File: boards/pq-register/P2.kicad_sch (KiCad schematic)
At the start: 36 parts, among them Q12 T1-N652, Q13 T1-N652, Q14 T1-N652, Q15 T1-N652, Q16 T1-N652, Q17 T1-N652

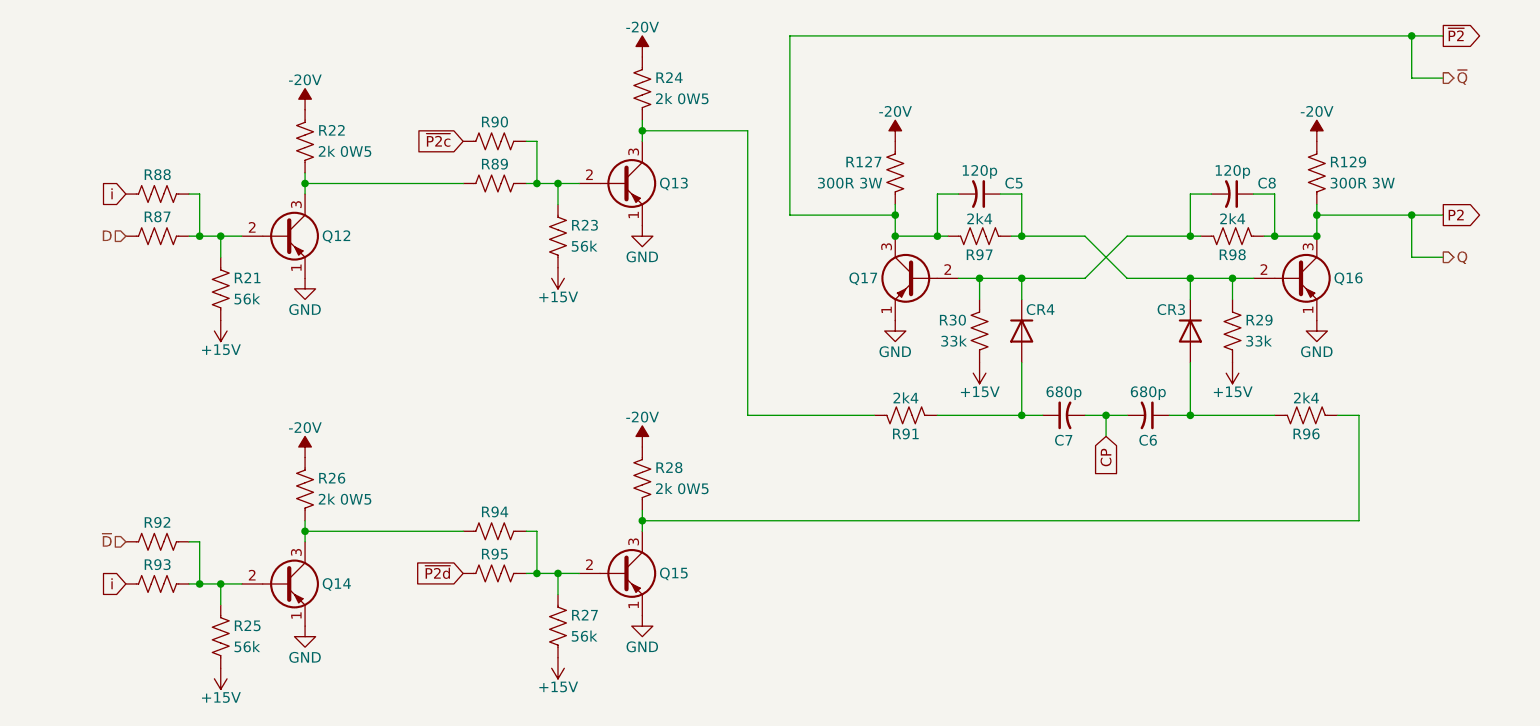
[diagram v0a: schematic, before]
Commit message: Run ERC and clean up P & Q Register board.
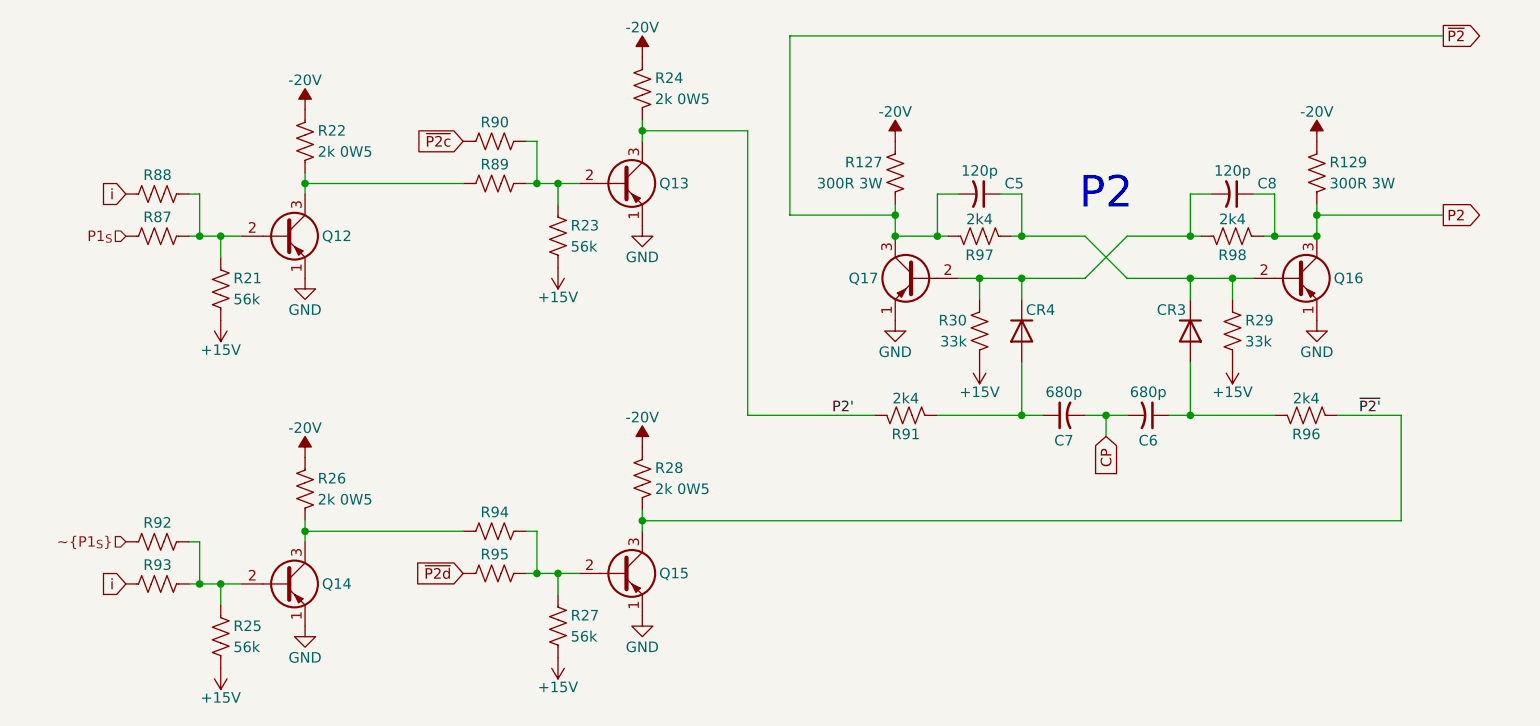
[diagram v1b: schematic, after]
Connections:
- net P2': now reaches Q13.3 (C), R24.2, R91.1
- net ~{P2'}: now reaches Q15.3 (C), R28.2, R96.2
- net D renamed P1_{S}
- net ~{D} renamed ~{P1_{S}}
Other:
- note added: "P2"
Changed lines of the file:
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@@
 		(title "LGP-21 P & Q Register Board")
 	)
+	(text "P2"
+		(exclude_from_sim no)
+		(at 177.8 82.55 0)
+		(effects
+			(font
+				(size 3.81 3.81)
+			)
+		)
+	)
 	(junction
 		(at 187.96 109.22)
@@
 	)
 	(junction
-		(at 214.63 85.09)
-		(diameter 0)
-		(color 0 0 0 0)
-	)
-	(junction
 		(at 167.64 87.63)
 		(diameter 0)
@@
 	)
 	(junction
-		(at 214.63 63.5)
-		(diameter 0)
-		(color 0 0 0 0)
-	)
-	(junction
 		(at 162.56 92.71)
 		(diameter 0)
@@
 	(wire
 		(pts
-			(xy 218.44 68.58) (xy 214.63 68.58)
-		)
-		(stroke
-			(width 0)
-			(type default)
-		)
-	)
-	(wire
-		(pts
 			(xy 180.34 87.63) (xy 187.96 87.63)
 		)
@@
 	(wire
 		(pts
-			(xy 218.44 90.17) (xy 214.63 90.17)
-		)
-		(stroke
-			(width 0)
-			(type default)
-		)
-	)
-	(wire
-		(pts
 			(xy 68.58 129.54) (xy 71.12 129.54)
 		)
@@
 	(wire
 		(pts
-			(xy 214.63 63.5) (xy 139.7 63.5)
+			(xy 139.7 63.5) (xy 218.44 63.5)
 		)
 		(stroke
@@
 	(wire
 		(pts
-			(xy 218.44 63.5) (xy 214.63 63.5)
-		)
-		(stroke
-			(width 0)
-			(type default)
-		)
-	)
-	(wire
-		(pts
 			(xy 139.7 63.5) (xy 139.7 85.09)
 		)
@@
 	(wire
 		(pts
-			(xy 214.63 85.09) (xy 218.44 85.09)
+			(xy 203.2 85.09) (xy 218.44 85.09)
 		)
 		(stroke
@@
 	(wire
 		(pts
-			(xy 208.28 109.22) (xy 208.28 121.92)
-		)
-		(stroke
-			(width 0)
-			(type default)
-		)
-	)
-	(wire
-		(pts
-			(xy 121.92 121.92) (xy 208.28 121.92)
+			(xy 213.36 109.22) (xy 213.36 121.92)
+		)
+		(stroke
+			(width 0)
+			(type default)
+		)
+	)
+	(wire
+		(pts
+			(xy 121.92 121.92) (xy 213.36 121.92)
 		)
 		(stroke
@@
 	(wire
 		(pts
-			(xy 203.2 85.09) (xy 214.63 85.09)
-		)
-		(stroke
-			(width 0)
-			(type default)
-		)
-	)
-	(wire
-		(pts
 			(xy 67.31 129.54) (xy 68.58 129.54)
 		)
@@
 	(wire
 		(pts
-			(xy 214.63 90.17) (xy 214.63 85.09)
-		)
-		(stroke
-			(width 0)
-			(type default)
-		)
-	)
-	(wire
-		(pts
-			(xy 214.63 68.58) (xy 214.63 63.5)
-		)
-		(stroke
-			(width 0)
-			(type default)
-		)
-	)
-	(wire
-		(pts
 			(xy 109.22 128.27) (xy 111.76 128.27)
 		)
@@
 	(wire
 		(pts
-			(xy 205.74 109.22) (xy 208.28 109.22)
+			(xy 205.74 109.22) (xy 213.36 109.22)
 		)
 		(stroke
@@
 			(width 0)
 			(type default)
+		)
+	)
+	(label "~{P2'}"
+		(at 208.28 109.22 0)
+		(effects
+			(font
+				(size 1.27 1.27)
+			)
+			(justify left bottom)
+		)
+	)
+	(label "P2'"
+		(at 144.78 109.22 0)
+		(effects
+			(font
+				(size 1.27 1.27)
+			)
+			(justify left bottom)
 		)
 	)
@@
 		)
 	)
-	(hierarchical_label "~{D}"
+	(hierarchical_label "~{P1_{S}}"
 		(shape input)
 		(at 59.69 124.46 180)
@@
 		)
 	)
-	(hierarchical_label "D"
+	(hierarchical_label "P1_{S}"
 		(shape input)
 		(at 59.69 87.63 180)
@@
 		)
 	)
-	(hierarchical_label "~{Q}"
-		(shape output)
-		(at 218.44 68.58 0)
-		(effects
-			(font
-				(size 1.27 1.27)
-			)
-			(justify left)
-		)
-	)
-	(hierarchical_label "Q"
-		(shape output)
-		(at 218.44 90.17 0)
-		(effects
-			(font
-				(size 1.27 1.27)
-			)
-			(justify left)
-		)
-	)

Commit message: Add copyright information.
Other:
- company: (none) -> © 1962 General Precision; redrawn by Sam Hanes
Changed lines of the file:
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@@
 	(title_block
 		(title "LGP-21 P & Q Register Board")
+		(date "2026-06-15")
+		(rev "ESD 1060")
+		(company "© 1962 General Precision; redrawn by Sam Hanes")
+		(comment 1 "https://github.com/Elemecca/lgp21-docs")
 	)
 	(text "P2"
